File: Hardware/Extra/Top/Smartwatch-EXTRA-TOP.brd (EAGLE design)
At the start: 38 x 38 mm, 64 parts, among them U1 NRF52832_MODULE_MDBT42, U3 FT231XS, U4 PHOTOTRANSISTOR, U5 MCP9808-MSOP8

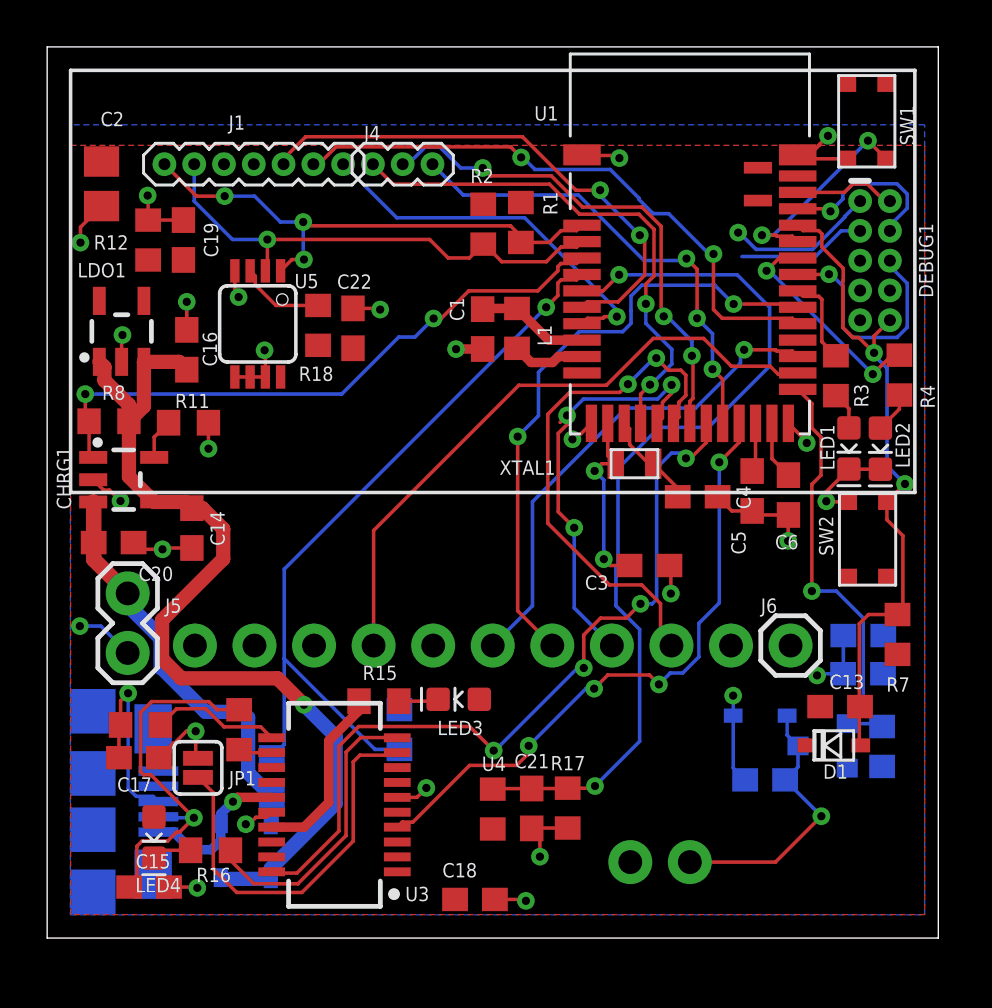
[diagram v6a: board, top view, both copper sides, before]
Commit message: GPS Removed, added back original display, kept pads for adafruit display
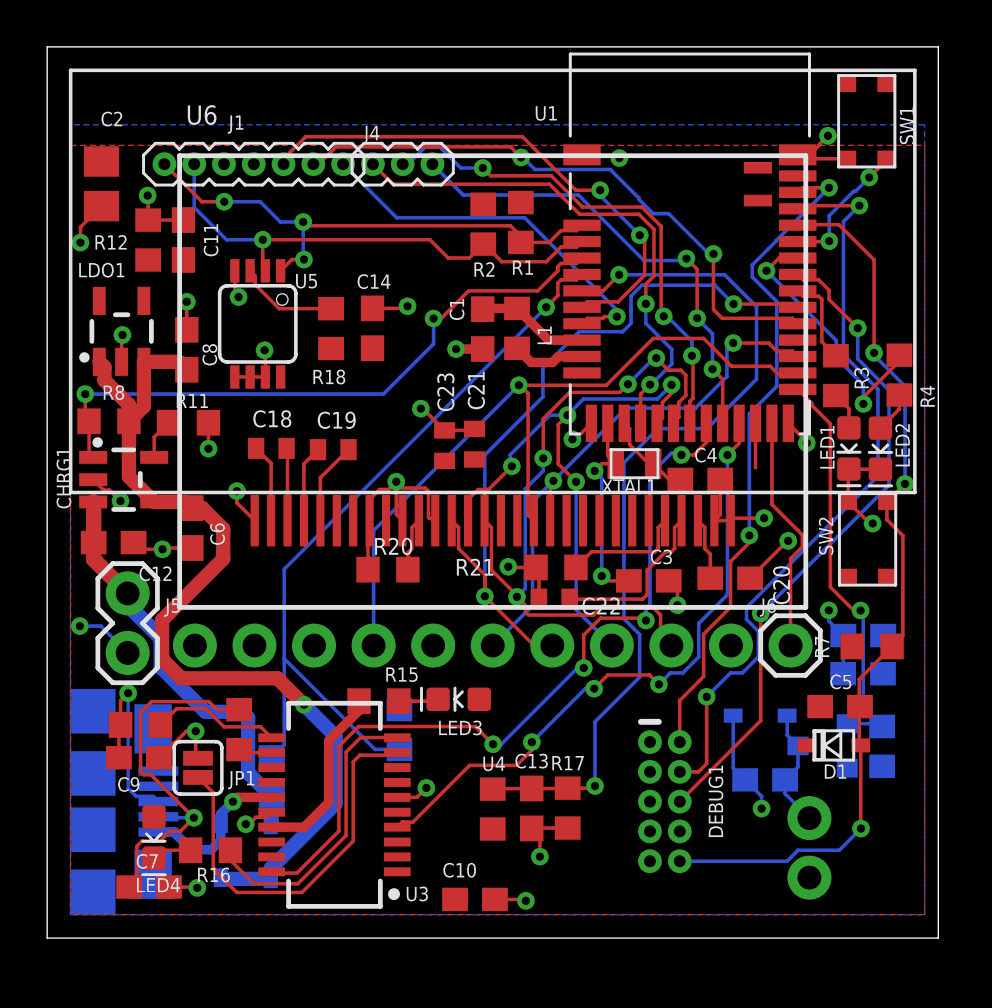
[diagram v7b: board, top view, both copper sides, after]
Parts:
- removed C24: 1u, LinnesLab-Passives:C0603
- removed C25: 100n, LinnesLab-Passives:C0603
- added C10: 100nF, LinnesLab-Passives:C0603
- added C11, C8: 1uF, LinnesLab-Passives:C0603
- added C12: 4.7uF, LinnesLab-Passives:C0603
- added C7, C9: 47pF, LinnesLab-Passives:C0603
- added R20: 10k, LinnesLab-Passives:R0603
- added R21: 390k, LinnesLab-Passives:R0603
- added U6: (no value), LinnesLab-Displays:UG-2864HSWEG01_0.96IN_NO-WRAPAROUND
- C1, C16: value 1u -> 1uF
- C13: value 100n -> 2.2uF
- C14: value 4.7u -> 100nF
- C15: value 47p -> 10pF
- C17: value 47p -> 100nF
- C18, C22: value 100n -> 2.2uF; device LinnesLab-Passives:C0603 -> LinnesLab-Passives:C0402
- C19: value 1u -> 2.2uF; device LinnesLab-Passives:C0603 -> LinnesLab-Passives:C0402
- C20: value 4.7u -> 10uF
- C21: device LinnesLab-Passives:C0603 -> LinnesLab-Passives:C0402
- C23: value 10pF -> 2.2uF; device LinnesLab-Passives:C0603 -> LinnesLab-Passives:C0402
- C5: value 300p -> 100nF
- C6: value 300p -> 4.7uF
- moved C16 32.0 mm to (34.8, 11.3), flipped to the bottom, turned to 180 degrees
- moved C17 31.3 mm to (34.8, 12.9), flipped to the bottom, turned to 180 degrees
- moved C15 26.7 mm to (30.6, 6.74), flipped to the bottom, turned to 0 degrees
- moved C20 26.3 mm to (29.1, 15.3), turned to 180 degrees
- moved C6 25.5 mm to (6.17, 17.5), turned to 90 degrees
- moved DEBUG1 24.7 mm to (26.3, 5.82)
- moved C18 21.1 mm to (9.56, 20.9)
- moved C23 19.7 mm to (16.9, 21.0), flipped to the top, turned to 270 degrees
- moved C21 15.7 mm to (18.2, 21.1)
- moved C22 14.4 mm to (21.6, 14.5), turned to 0 degrees
- moved C13 13.8 mm to (20.7, 5.53), turned to 270 degrees
- moved C14 11.5 mm to (13.9, 26.0)
- moved C19 11.0 mm to (12.2, 20.8), turned to 180 degrees
- moved C5 9.93 mm to (33.8, 9.87), turned to 0 degrees
- moved M1 6.40 mm to (32.5, 3.85), turned to 90 degrees
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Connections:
- removed net LIT: J6.1
- removed net P0.10/NFC2: C6.1, U1.23
- new net D10/LIT: J6.1, U1.23
- new net N$13: C18.1, U6.3
- new net N$15: C19.2, U6.4
- new net N$17: C19.1, U6.5
- new net N$19: C20.2, U6.28
- new net N$20: C22.2, U6.27
- new net N$5: R20.2, U6.11
- new net N$7: R21.1, U6.26
- new net N$8: C18.2, U6.2
- net 3.3V: now also C10.2, C11.1, C14.1, C15.2, C16.1, C17.1, C21.2, U6.6, U6.9; no longer C18.2, C19.1, C22.1, C24.1, C25.1
- net A5/LIGHT: now also C13.1; no longer C21.1
- net D16/CS.OLED: now also U6.13
- net D3/RESET.OLED: now also U6.14
- net D4/DC.OLED: now also U6.15
- net DTR: now also C5.1; no longer C13.1
- net GND: now also C10.1, C11.2, C12.2, C13.2, C14.2, C16.2, C20.1, C21.1, C22.1, C23.1, C6.1, C7.1, C8.1, C9.2, R20.1, R21.2, U6.1, U6.10, U6.12, U6.29, U6.30, U6.8; no longer C14.1, C15.1, C16.1, C18.1, C19.2, C20.2, C21.2, C22.2, C24.2, C25.2, C5.2, C6.2
- net MOSI: now also U6.19
- net N$18: now also C15.1; no longer C23.1
- net P0.09/NFC1: no longer C5.1
- net RESET: now also C5.2; no longer C13.2
- net SCK: now also U6.18
- net USB+: now also C9.1; no longer C17.1
- net USB-: now also C7.2; no longer C15.2
- net VIN: now also C6.2, C8.2; no longer C14.2, C16.2
- net VLIPO: now also C12.1; no longer C20.1
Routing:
- net SWCLK: track 7.38 -> 32.4 mm, vias 1 -> 2
- net SWDIO: track 4.39 -> 28.6 mm, vias 0 -> 2
- net SWO: track 10.1 -> 28.2 mm, vias 1 -> 2
- net GND: track 55.3 -> 68.8 mm, vias 25 -> 30
- net D10/LIT: track 0.00 -> 10.2 mm
- net RESET: track 28.5 -> 38.4 mm, vias 2 -> 3
- net D4/DC.OLED: track 22.3 -> 30.0 mm, vias 2 -> 4
- net N$20: track 0.00 -> 7.30 mm
- net D3/RESET.OLED: track 18.2 -> 24.8 mm, vias 3 -> 4
- net N$18: track 11.8 -> 5.22 mm, vias 1 -> 0
- net SCK: track 27.0 -> 33.0 mm, vias 0 -> 1
- net 3.3V: track 13.0 -> 7.43 mm, vias 3 -> 2
- net D16/CS.OLED: track 26.3 -> 31.7 mm
- net N$7: track 0.00 -> 5.16 mm
- net N$17: track 0.00 -> 3.52 mm
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
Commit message: Silkscreens fixed, Airwires removed
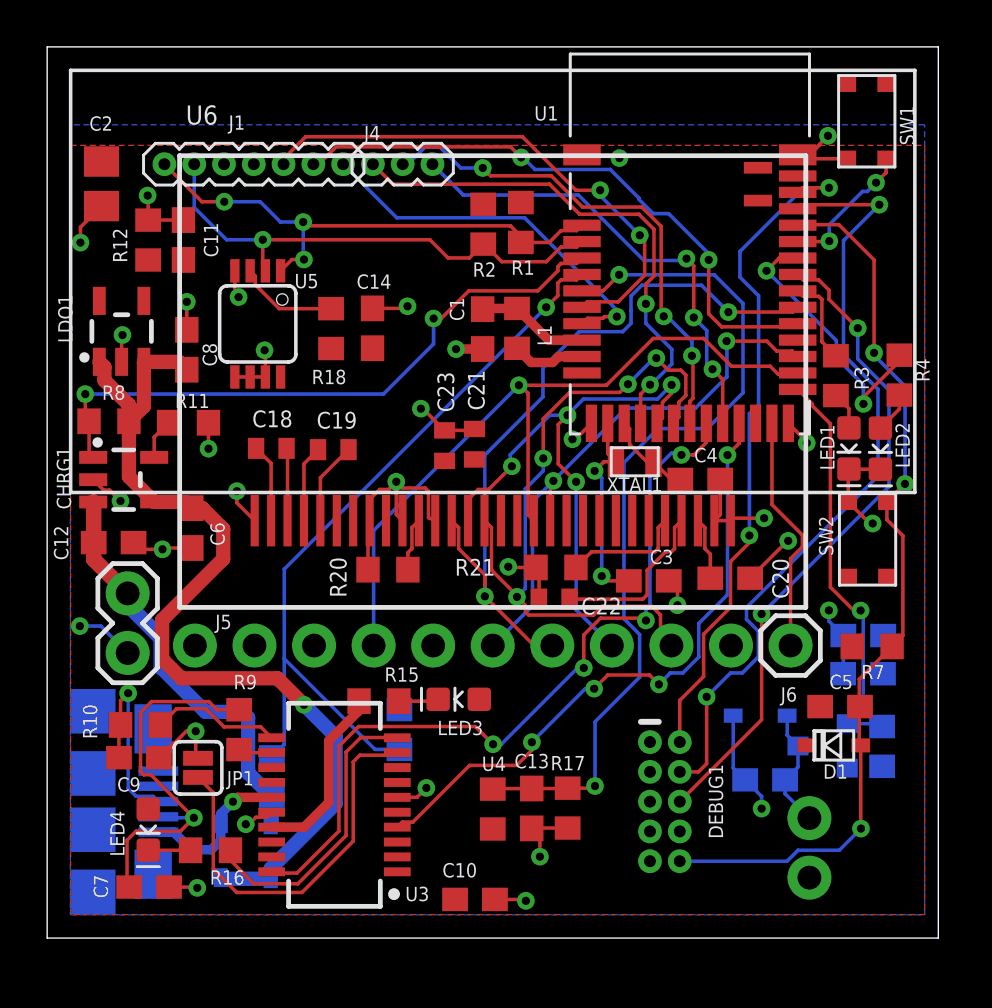
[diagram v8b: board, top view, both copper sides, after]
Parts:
- moved LED4 0.42 mm to (4.31, 4.63)
- moved XTAL1 0.08 mm to (25.1, 20.3)
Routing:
- net P0.09/NFC1: track 1.89 -> 0.00 mm
- net SWCLK: track 32.4 -> 33.7 mm
- net A5/LIGHT: track 37.8 -> 37.0 mm
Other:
- board text added: "R10"
- board text added: "R9"
